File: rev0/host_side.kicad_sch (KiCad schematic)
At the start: 21 parts, among them IC1 ECP5-BGA256, U11 USB3343-CP

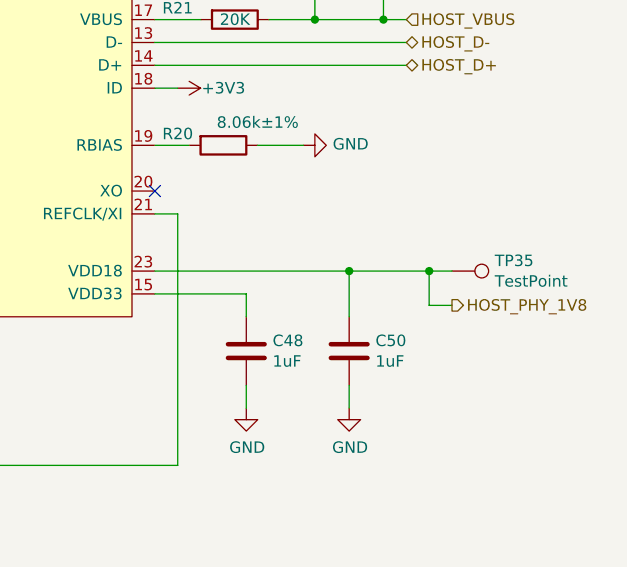
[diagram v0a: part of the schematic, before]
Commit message: hardware: remove PHY 1.8 V measurement
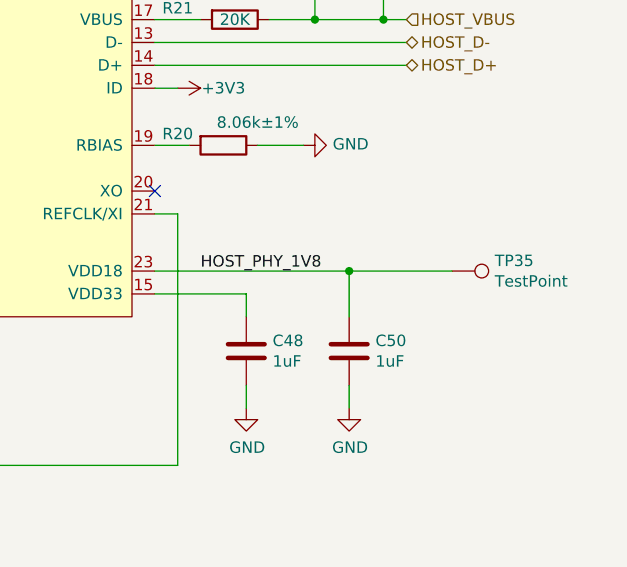
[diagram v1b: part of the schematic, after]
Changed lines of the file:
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@@
   (junction (at 118.11 38.1) (diameter 0) (color 0 0 0 0)
-  )
-  (junction (at 257.81 96.52) (diameter 0) (color 0 0 0 0)
   )
   (junction (at 111.76 33.02) (diameter 0) (color 0 0 0 0)
@@
     (stroke (width 0) (type default) (color 0 0 0 0))
   )
-  (wire (pts (xy 260.35 100.33) (xy 257.81 100.33))
-    (stroke (width 0) (type default) (color 0 0 0 0))
-  )
   (wire (pts (xy 237.49 111.76) (xy 237.49 109.22))
     (stroke (width 0) (type default) (color 0 0 0 0))
@@
     (stroke (width 0) (type default) (color 0 0 0 0))
   )
-  (wire (pts (xy 248.92 96.52) (xy 257.81 96.52))
-    (stroke (width 0) (type default) (color 0 0 0 0))
-  )
   (bus (pts (xy 148.59 63.5) (xy 148.59 66.04))
     (stroke (width 0) (type default) (color 0 0 0 0))
@@
     (stroke (width 0) (type default) (color 0 0 0 0))
   )
-  (wire (pts (xy 257.81 96.52) (xy 260.35 96.52))
-    (stroke (width 0) (type default) (color 0 0 0 0))
-  )
-  (wire (pts (xy 257.81 100.33) (xy 257.81 96.52))
+  (wire (pts (xy 248.92 96.52) (xy 260.35 96.52))
     (stroke (width 0) (type default) (color 0 0 0 0))
   )
@@
   (label "HOST_DATA2" (at 190.5 63.5 180)
     (effects (font (size 1.27 1.27)) (justify right bottom))
+  )
+  (label "HOST_PHY_1V8" (at 232.41 96.52 0)
+    (effects (font (size 1.27 1.27)) (justify left bottom))
   )
   (label "HOST_DATA5" (at 190.5 71.12 180)
@@
     (effects (font (size 1.27 1.27)) (justify left))
   )
-  (hierarchical_label "HOST_PHY_1V8" (shape output) (at 260.35 100.33 0)
-    (effects (font (size 1.27 1.27)) (justify left))
-  )

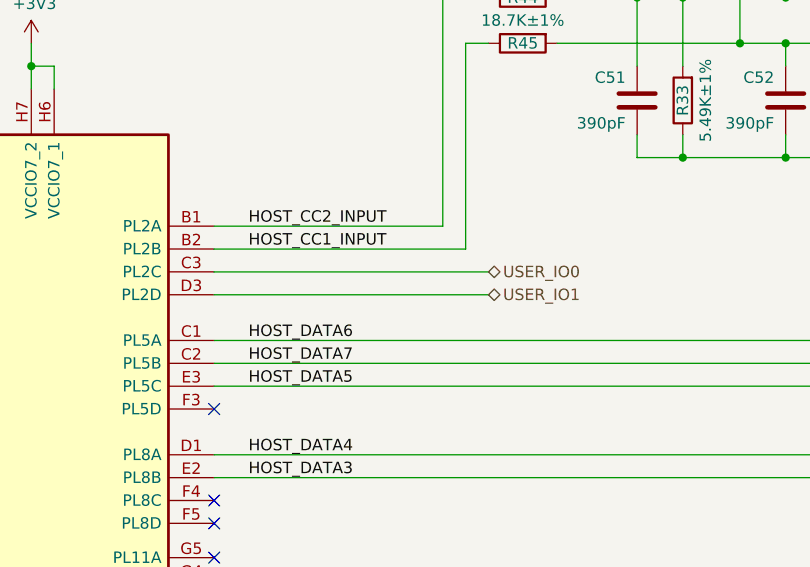
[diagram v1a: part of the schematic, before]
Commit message: hardware: remove user i/o SMA connectors
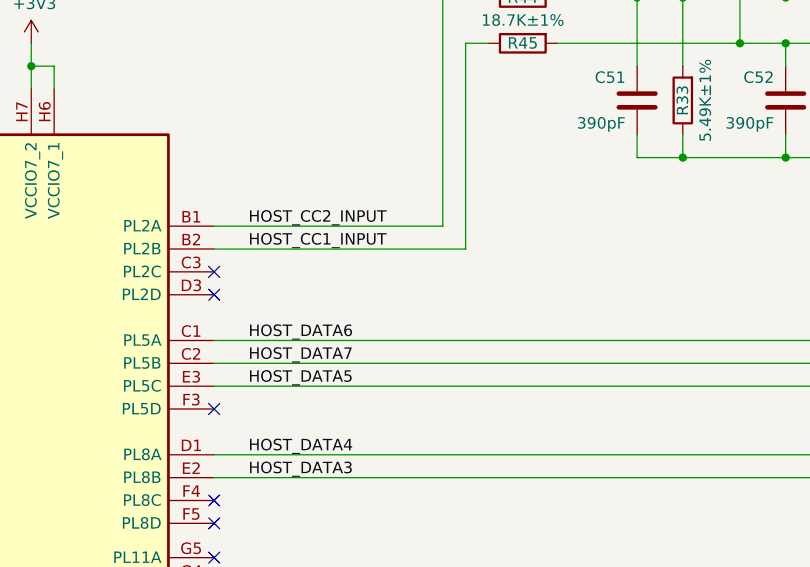
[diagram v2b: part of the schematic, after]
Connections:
- net USER_IO0: no longer names the net of IC1.C3 (PL2C)
- net USER_IO1: no longer names the net of IC1.D3 (PL2D)
- no-connect marks 14 -> 16
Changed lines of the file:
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@@
   (no_connect (at 59.69 88.9))
   (no_connect (at 59.69 113.03))
+  (no_connect (at 59.69 63.5))
   (no_connect (at 59.69 95.25))
   (no_connect (at 59.69 115.57))
   (no_connect (at 59.69 119.38))
   (no_connect (at 59.69 135.89))
+  (no_connect (at 59.69 66.04))
   (no_connect (at 59.69 124.46))
   (no_connect (at 59.69 78.74))
@@
     (stroke (width 0) (type default) (color 0 0 0 0))
   )
-  (wire (pts (xy 59.69 66.04) (xy 90.17 66.04))
-    (stroke (width 0) (type default) (color 0 0 0 0))
-  )
   (wire (pts (xy 252.73 68.58) (xy 255.27 68.58))
-    (stroke (width 0) (type default) (color 0 0 0 0))
-  )
-  (wire (pts (xy 90.17 63.5) (xy 59.69 63.5))
     (stroke (width 0) (type default) (color 0 0 0 0))
   )
@@
     (effects (font (size 1.27 1.27)) (justify left))
   )
-  (hierarchical_label "USER_IO0" (shape bidirectional) (at 90.17 63.5 0)
-    (effects (font (size 1.27 1.27)) (justify left))
-  )
-  (hierarchical_label "USER_IO1" (shape bidirectional) (at 90.17 66.04 0)
-    (effects (font (size 1.27 1.27)) (justify left))
-  )

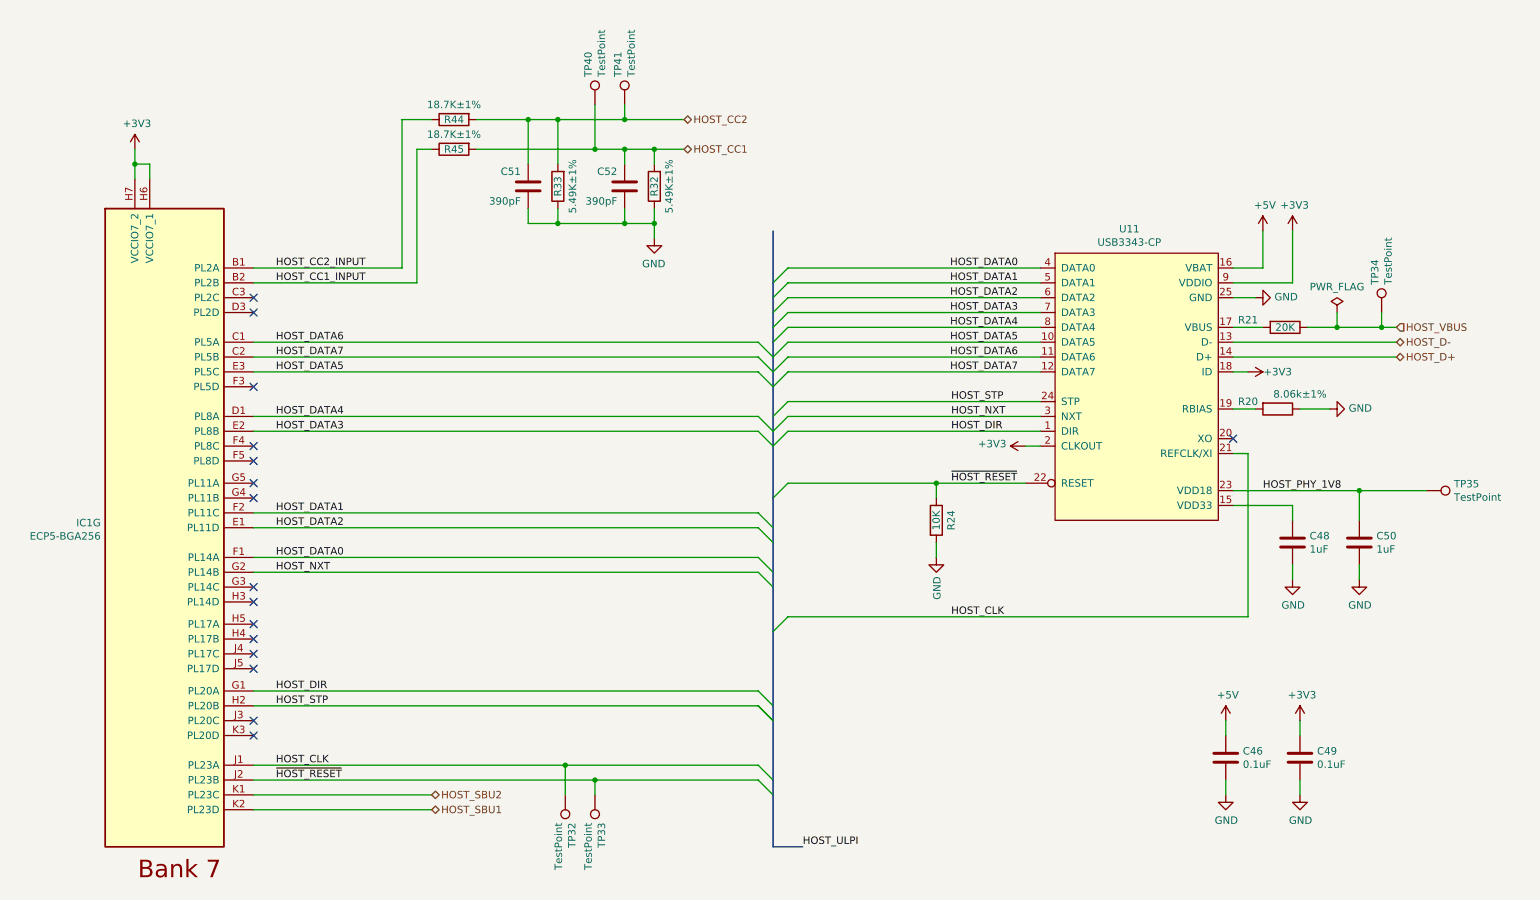
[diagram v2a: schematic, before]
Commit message: hardware: rename buses for KiCad 6
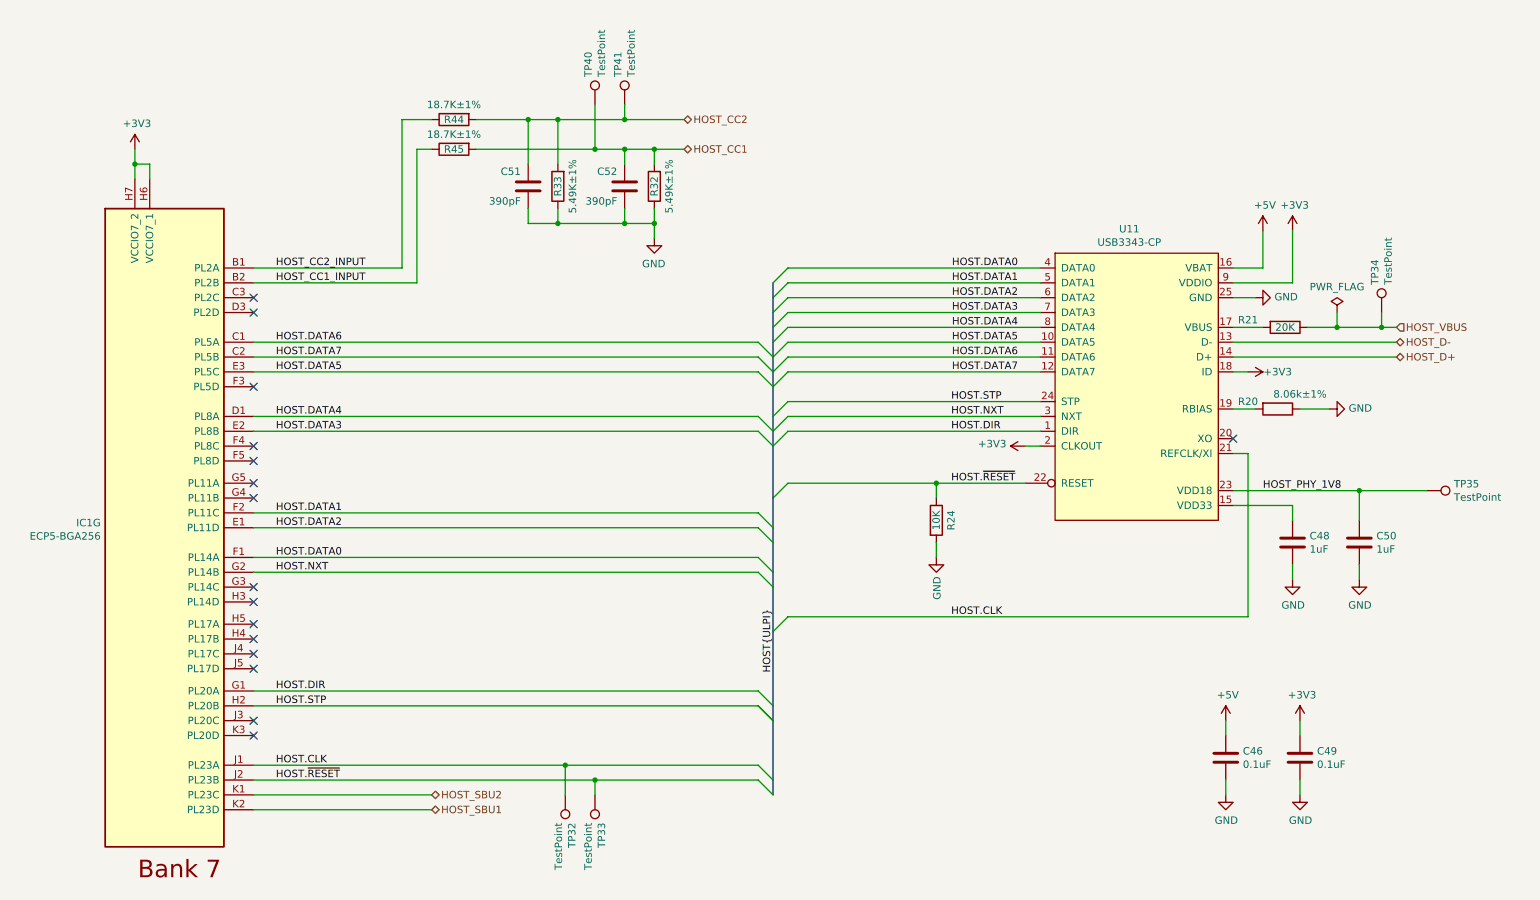
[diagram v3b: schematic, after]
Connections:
- net HOST_CLK renamed HOST.CLK
- net HOST_DATA0 renamed HOST.DATA0
- net HOST_DATA1 renamed HOST.DATA1
- net HOST_DATA2 renamed HOST.DATA2
- net HOST_DATA3 renamed HOST.DATA3
- net HOST_DATA4 renamed HOST.DATA4
- net HOST_DATA5 renamed HOST.DATA5
- net HOST_DATA6 renamed HOST.DATA6
- net HOST_DATA7 renamed HOST.DATA7
- net HOST_DIR renamed HOST.DIR
- net HOST_NXT renamed HOST.NXT
- net HOST_STP renamed HOST.STP
- net ~{HOST_RESET} renamed HOST.~{RESET}
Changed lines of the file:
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@@
-    (stroke (width 0) (type default) (color 0 0 0 0))
-  )
-  (bus (pts (xy 148.59 52.07) (xy 148.59 60.96))
     (stroke (width 0) (type default) (color 0 0 0 0))
   )
@@
     (stroke (width 0) (type default) (color 0 0 0 0))
   )
-  (bus (pts (xy 148.59 148.59) (xy 148.59 157.48))
-    (stroke (width 0) (type default) (color 0 0 0 0))
-  )
   (wire (pts (xy 59.69 107.95) (xy 146.05 107.95))
     (stroke (width 0) (type default) (color 0 0 0 0))
@@
     (stroke (width 0) (type default) (color 0 0 0 0))
   )
-  (bus (pts (xy 148.59 157.48) (xy 153.67 157.48))
-    (stroke (width 0) (type default) (color 0 0 0 0))
-  )
   (wire (pts (xy 227.33 71.12) (xy 255.27 71.12))
     (stroke (width 0) (type default) (color 0 0 0 0))
@@
     (stroke (width 0) (type default) (color 0 0 0 0))
   )
-  (label "HOST_DATA1" (at 63.5 100.33 0)
+  (label "HOST.DATA1" (at 63.5 100.33 0)
     (effects (font (size 1.27 1.27)) (justify left bottom))
   )
@@
     (effects (font (size 1.27 1.27)) (justify left bottom))
   )
-  (label "~{HOST_RESET}" (at 63.5 146.05 0)
-    (effects (font (size 1.27 1.27)) (justify left bottom))
-  )
-  (label "~{HOST_RESET}" (at 179.07 95.25 0)
-    (effects (font (size 1.27 1.27)) (justify left bottom))
-  )
-  (label "HOST_DIR" (at 179.07 86.36 0)
-    (effects (font (size 1.27 1.27)) (justify left bottom))
-  )
-  (label "HOST_STP" (at 179.07 81.28 0)
-    (effects (font (size 1.27 1.27)) (justify left bottom))
-  )
-  (label "HOST_DATA5" (at 63.5 76.2 0)
-    (effects (font (size 1.27 1.27)) (justify left bottom))
-  )
-  (label "HOST_DATA7" (at 190.5 76.2 180)
-    (effects (font (size 1.27 1.27)) (justify right bottom))
-  )
-  (label "HOST_DATA6" (at 190.5 73.66 180)
-    (effects (font (size 1.27 1.27)) (justify right bottom))
-  )
-  (label "HOST_STP" (at 63.5 133.35 0)
-    (effects (font (size 1.27 1.27)) (justify left bottom))
-  )
-  (label "HOST_DIR" (at 63.5 130.81 0)
-    (effects (font (size 1.27 1.27)) (justify left bottom))
-  )
-  (label "HOST_DATA7" (at 63.5 73.66 0)
-    (effects (font (size 1.27 1.27)) (justify left bottom))
-  )
-  (label "HOST_DATA3" (at 63.5 86.36 0)
-    (effects (font (size 1.27 1.27)) (justify left bottom))
-  )
-  (label "HOST_CLK" (at 63.5 143.51 0)
-    (effects (font (size 1.27 1.27)) (justify left bottom))
-  )
-  (label "HOST_CLK" (at 179.07 118.11 0)
-    (effects (font (size 1.27 1.27)) (justify left bottom))
-  )
-  (label "HOST_DATA3" (at 190.5 66.04 180)
-    (effects (font (size 1.27 1.27)) (justify right bottom))
-  )
-  (label "HOST_DATA6" (at 63.5 71.12 0)
-    (effects (font (size 1.27 1.27)) (justify left bottom))
-  )
-  (label "HOST_DATA2" (at 63.5 102.87 0)
-    (effects (font (size 1.27 1.27)) (justify left bottom))
-  )
-  (label "HOST_DATA0" (at 63.5 107.95 0)
-    (effects (font (size 1.27 1.27)) (justify left bottom))
-  )
-  (label "HOST_DATA1" (at 190.5 60.96 180)
-    (effects (font (size 1.27 1.27)) (justify right bottom))
-  )
-  (label "HOST_DATA4" (at 63.5 83.82 0)
-    (effects (font (size 1.27 1.27)) (justify left bottom))
-  )
-  (label "HOST_ULPI" (at 153.67 157.48 0)
-    (effects (font (size 1.27 1.27)) (justify left bottom))
-  )
-  (label "HOST_DATA4" (at 190.5 68.58 180)
-    (effects (font (size 1.27 1.27)) (justify right bottom))
-  )
-  (label "HOST_DATA2" (at 190.5 63.5 180)
+  (label "HOST.~{RESET}" (at 63.5 146.05 0)
+    (effects (font (size 1.27 1.27)) (justify left bottom))
+  )
+  (label "HOST.~{RESET}" (at 179.07 95.25 0)
+    (effects (font (size 1.27 1.27)) (justify left bottom))
+  )
+  (label "HOST.DIR" (at 179.07 86.36 0)
+    (effects (font (size 1.27 1.27)) (justify left bottom))
+  )
+  (label "HOST.STP" (at 179.07 81.28 0)
+    (effects (font (size 1.27 1.27)) (justify left bottom))
+  )
+  (label "HOST.DATA5" (at 63.5 76.2 0)
+    (effects (font (size 1.27 1.27)) (justify left bottom))
+  )
+  (label "HOST.DATA7" (at 190.5 76.2 180)
+    (effects (font (size 1.27 1.27)) (justify right bottom))
+  )
+  (label "HOST.DATA6" (at 190.5 73.66 180)
+    (effects (font (size 1.27 1.27)) (justify right bottom))
+  )
+  (label "HOST.STP" (at 63.5 133.35 0)
+    (effects (font (size 1.27 1.27)) (justify left bottom))
+  )
+  (label "HOST.DIR" (at 63.5 130.81 0)
+    (effects (font (size 1.27 1.27)) (justify left bottom))
+  )
+  (label "HOST.DATA7" (at 63.5 73.66 0)
+    (effects (font (size 1.27 1.27)) (justify left bottom))
+  )
+  (label "HOST.DATA3" (at 63.5 86.36 0)
+    (effects (font (size 1.27 1.27)) (justify left bottom))
+  )
+  (label "HOST{ULPI}" (at 148.59 127.635 90)
+    (effects (font (size 1.27 1.27)) (justify left bottom))
+  )
+  (label "HOST.CLK" (at 63.5 143.51 0)
+    (effects (font (size 1.27 1.27)) (justify left bottom))
+  )
+  (label "HOST.CLK" (at 179.07 118.11 0)
+    (effects (font (size 1.27 1.27)) (justify left bottom))
+  )
+  (label "HOST.DATA3" (at 190.5 66.04 180)
+    (effects (font (size 1.27 1.27)) (justify right bottom))
+  )
+  (label "HOST.DATA6" (at 63.5 71.12 0)
+    (effects (font (size 1.27 1.27)) (justify left bottom))
+  )
+  (label "HOST.DATA2" (at 63.5 102.87 0)
+    (effects (font (size 1.27 1.27)) (justify left bottom))
+  )
+  (label "HOST.DATA0" (at 63.5 107.95 0)
+    (effects (font (size 1.27 1.27)) (justify left bottom))
+  )
+  (label "HOST.DATA1" (at 190.5 60.96 180)
+    (effects (font (size 1.27 1.27)) (justify right bottom))
+  )
+  (label "HOST.DATA4" (at 63.5 83.82 0)
+    (effects (font (size 1.27 1.27)) (justify left bottom))
+  )
+  (label "HOST.DATA4" (at 190.5 68.58 180)
+    (effects (font (size 1.27 1.27)) (justify right bottom))
+  )
+  (label "HOST.DATA2" (at 190.5 63.5 180)
     (effects (font (size 1.27 1.27)) (justify right bottom))
   )
@@
     (effects (font (size 1.27 1.27)) (justify left bottom))
   )
-  (label "HOST_DATA5" (at 190.5 71.12 180)
-    (effects (font (size 1.27 1.27)) (justify right bottom))
-  )
-  (label "HOST_NXT" (at 179.07 83.82 0)
-    (effects (font (size 1.27 1.27)) (justify left bottom))
-  )
-  (label "HOST_NXT" (at 63.5 110.49 0)
+  (label "HOST.DATA5" (at 190.5 71.12 180)
+    (effects (font (size 1.27 1.27)) (justify right bottom))
+  )
+  (label "HOST.NXT" (at 179.07 83.82 0)
+    (effects (font (size 1.27 1.27)) (justify left bottom))
+  )
+  (label "HOST.NXT" (at 63.5 110.49 0)
     (effects (font (size 1.27 1.27)) (justify left bottom))
   )
@@
     (effects (font (size 1.27 1.27)) (justify left bottom))
   )
-  (label "HOST_DATA0" (at 190.5 58.42 180)
-    (effects (font (size 1.27 1.27)) (justify right bottom))
-  )
+  (label "HOST.DATA0" (at 190.5 58.42 180)
+    (effects (font (size 1.27 1.27)) (justify right bottom))
+  )

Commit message: hardware: use DNP field for DNP notation
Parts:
- TP32, TP33, TP34, TP35, TP40, TP41: DNP (none) -> DNP; Note DNP -> (none)
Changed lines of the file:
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@@
       (effects (font (size 1.27 1.27)) hide)
     )
-    (property "Note" "DNP" (id 4) (at 118.11 30.48 0)
+    (property "DNP" "DNP" (id 4) (at 118.11 30.48 0)
       (effects (font (size 1.27 1.27)) hide)
     )
@@
       (effects (font (size 1.27 1.27)) hide)
     )
-    (property "Note" "DNP" (id 4) (at 123.19 30.48 0)
+    (property "DNP" "DNP" (id 4) (at 123.19 30.48 0)
       (effects (font (size 1.27 1.27)) hide)
     )
@@
       (effects (font (size 1.27 1.27)) hide)
     )
-    (property "Note" "DNP" (id 4) (at 260.35 96.52 0)
+    (property "DNP" "DNP" (id 4) (at 260.35 96.52 0)
       (effects (font (size 1.27 1.27)) hide)
     )
@@
       (effects (font (size 1.27 1.27)) hide)
     )
-    (property "Note" "DNP" (id 4) (at 252.73 66.04 0)
+    (property "DNP" "DNP" (id 4) (at 252.73 66.04 0)
       (effects (font (size 1.27 1.27)) hide)
     )
@@
       (effects (font (size 1.27 1.27)) hide)
     )
-    (property "Note" "DNP" (id 4) (at 118.11 148.59 0)
+    (property "DNP" "DNP" (id 4) (at 118.11 148.59 0)
       (effects (font (size 1.27 1.27)) hide)
     )
@@
       (effects (font (size 1.27 1.27)) hide)
     )
-    (property "Note" "DNP" (id 4) (at 113.03 148.59 0)
+    (property "DNP" "DNP" (id 4) (at 113.03 148.59 0)
       (effects (font (size 1.27 1.27)) hide)
     )
